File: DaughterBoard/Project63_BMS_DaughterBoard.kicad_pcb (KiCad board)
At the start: 4 copper layers, 166 parts, among them J1 430450200, J4 1-794106-0, J5 430450200, Q1 ZXTN4004KTC, U1 BQ79614PAPRQ1

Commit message: Initial Routing
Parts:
- D1, D2: footprint PESD1CAN,215:SOT23_PESD1_NEX -> PESD1CAN_215:SOT23_PESD1_NEX
- moved TP5 5.40 mm to (157.5, 76.2)
- turned R28 to 0 degrees
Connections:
- C3 pad 2: REFHF -> REFHP
- F30 pad 1: Cell 14S -> BAT
- J4 pad 18: Cell 14S -> BAT
- R1 pad 2: Cell 14S -> BAT
- R33 pad 2: Cell 14S -> BAT
- U1 pad 36: REFHP -> AVSS
- U1 pad 37: REFHF -> REFHP
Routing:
- net BAT: track 0.00 -> 133.5 mm, vias 0 -> 2
- net Cell 0: track 0.00 -> 102.9 mm
- net VC0: track 0.00 -> 67.3 mm
- net Cell 14: track 0.00 -> 55.0 mm, vias 0 -> 1
- net VC1: track 0.00 -> 52.3 mm
- net VC2: track 0.00 -> 45.2 mm
- net Cell 6: track 0.00 -> 43.1 mm, vias 0 -> 2
- net Net-(F2-Pad2): track 0.00 -> 42.1 mm
- net Net-(F1-Pad2): track 0.00 -> 42.1 mm
- net Net-(F15-Pad2): track 0.00 -> 40.3 mm
- net Net-(F3-Pad2): track 0.00 -> 39.7 mm
- net VC3: track 0.00 -> 39.2 mm
- net Net-(F14-Pad2): track 0.00 -> 39.1 mm
- net Net-(F4-Pad2): track 0.00 -> 35.7 mm
- net Net-(F13-Pad2): track 0.00 -> 34.8 mm
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
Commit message: Routing update 2
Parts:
- moved TP6 50.1 mm to (160.0, 68.6)
- moved J4 35.6 mm to (55.0, 116.3)
- moved TP1 31.0 mm to (146.0, 73.3)
- moved R33 30.9 mm to (124.5, 55.9), turned to 180 degrees
- moved TP11 29.9 mm to (151.1, 73.3)
- moved R32 29.0 mm to (132.1, 55.9)
- moved R10 28.4 mm to (110.7, 123.2), turned to -90 degrees
- moved R2 28.4 mm to (110.6, 82.6), turned to -90 degrees
- moved R3 28.4 mm to (110.6, 87.7), turned to -90 degrees
- moved R4 28.4 mm to (110.6, 92.7), turned to -90 degrees
- moved R5 28.4 mm to (110.6, 97.8), turned to -90 degrees
- moved R6 28.4 mm to (110.6, 102.9), turned to -90 degrees
- moved R8 28.4 mm to (110.6, 113.1), turned to -90 degrees
- moved R9 28.4 mm to (110.6, 118.1), turned to -90 degrees
- moved R11 28.4 mm to (110.6, 128.3), turned to -90 degrees
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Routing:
- net CB0: track 0.00 -> 92.6 mm, vias 0 -> 2
- net CB1: track 0.00 -> 81.1 mm, vias 0 -> 2
- net CB2: track 0.00 -> 71.6 mm, vias 0 -> 2
- net CB3: track 0.00 -> 63.6 mm, vias 0 -> 2
- net CB4: track 0.00 -> 57.4 mm, vias 0 -> 2
- net CB5: track 0.00 -> 50.5 mm, vias 0 -> 2
- net CB6: track 0.00 -> 49.2 mm, vias 0 -> 2
- net CB7: track 0.00 -> 43.3 mm, vias 0 -> 2
- net CB14: track 0.00 -> 40.4 mm
- net CB13: track 0.00 -> 38.9 mm
- net CB9: track 0.00 -> 38.7 mm, vias 0 -> 2
- net CB8: track 0.00 -> 38.2 mm, vias 0 -> 2
- net Cell 0: track 102.9 -> 65.2 mm
- net CB12: track 0.00 -> 37.4 mm, vias 0 -> 2
- net CB11: track 0.00 -> 36.6 mm, vias 0 -> 2
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
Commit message: Routing Update 3
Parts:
- C10, C11, C12, C13, C14, C15, C16, C17, C18, C19, C2, C3, C31, C32, C33, C34, C4, C5, C6, C7, C9: moved to B.Cu
- R1: value 30 -> 30
- R10, R11, R12, R2, R24, R25, R26, R27, R3, R4, R5, R6, R7, R8, R9: value 7.5 -> 7.5
- R13, R14, R15, R16, R17, R18, R19, R20, R21, R22, R23, R28, R29, R30, R31, R32: value 100 -> 100
- R33: value 200 -> 200
- R34, R35, R41, R42: value 51 -> 51
- R37, R38, R39, R40, R43, R44, R45, R46, R47, R48, R50, R51, R52, R53, R54, R55: value 0 -> 0
- moved J1 52.1 mm to (210.8, 117.3)
- moved R44 49.2 mm to (213.4, 109.2)
- moved LDOIN 48.3 mm to (186.2, 35.3)
- moved R43 47.3 mm to (208.3, 109.2)
- moved R47 45.9 mm to (205.8, 103.5)
- moved FL1 45.4 mm to (210.7, 103.3)
- moved TSREF 45.1 mm to (190.5, 66.0)
- moved R42 44.8 mm to (213.2, 68.0)
- moved R48 44.8 mm to (215.8, 103.6)
- moved C43 44.6 mm to (213.3, 95.9)
- moved C44 44.5 mm to (208.1, 95.9)
- moved R39 43.3 mm to (213.2, 62.9)
- moved R45 43.0 mm to (208.2, 91.1)
- moved R46 43.0 mm to (213.3, 91.1)
- moved R38 42.3 mm to (208.2, 88.2)
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- renumbered TP7 to AVDD, TP5 to BAT, TP32 to CELL0, TP27 to CELL1, TP18 to CELL10, TP28 to CELL11, TP29 to CELL12, TP30 to CELL13, TP31 to CELL14, TP26 to CELL2, TP25 to CELL3, TP24 to CELL4, TP23 to CELL5, TP22 to CELL6, TP21 to CELL7, TP20 to CELL8, TP19 to CELL9, TP9 to CVDD, TP11 to DVDD, TP2 to LDOIN, TP3 to NEG5V, TP14 to NFAULT, TP4 to NPNB, TP6 to REFHP, TP1 to TSREF
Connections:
- net COMML_N_OPT renamed COMML_N_OPT-
- net COMML_P_OPT renamed COMML_P_OPT+
- C2 pad 1: AVSS -> CVSS
- C3 pad 1: AVSS -> REFHM
- C40 pad 1: AVSS -> CVSS
- C41 pad 1: AVSS -> CVSS
- C42 pad 1: AVSS -> CVSS
- C42 pad 2: COMHN -> COMHP
- C45 pad 1: AVSS -> CVSS
- C45 pad 2: COMHP -> COMHN
- C5 pad 1: AVSS -> CVSS
- C6 pad 1: AVSS -> CVSS
- C7 pad 1: AVSS -> DVSS
- C8 pad 1: AVSS -> CVSS
- D1 pad 3: AVSS -> CVSS
- D2 pad 3: AVSS -> CVSS
- R34 pad 2: Net-(D2-Pad1) -> Net-(D2-Pad2)
- R35 pad 2: Net-(D2-Pad2) -> Net-(D2-Pad1)
- R37 pad 2: Net-(D2-Pad2) -> Net-(D2-Pad1)
- R38 pad 2: Net-(D2-Pad1) -> Net-(D2-Pad2)
- R39 pad 1: COMMH_N_OPT -> COMMH_N_OPT-
- R40 pad 1: COMMH_P_OPT -> COMMH_P_OPT+
- R50 pad 2: ISO_COMMH_P -> ISO_COMMH_N
- R51 pad 2: ISO_COMMH_N -> ISO_COMMH_P
- R54 pad 1: COMMH_P_OPT -> COMMH_N_OPT-
- R55 pad 1: COMMH_N_OPT -> COMMH_P_OPT+
- U1 pad 36: AVSS -> REFHM
- U1 pad 46: AVSS -> CVSS
- U1 pad 50: AVSS -> DVSS
- U1 pad 62: unconnected-(U1-Pad62) -> NFAULT
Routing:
- net LDOIN: track 0.00 -> 43.0 mm, vias 0 -> 2
- net COMLN: track 0.00 -> 35.1 mm
- net COMHN: track 0.00 -> 34.9 mm
- net COMHP: track 0.00 -> 34.9 mm
- net COMLP: track 0.00 -> 34.9 mm
- net NPNB: track 7.31 -> 40.7 mm, vias 0 -> 2
- net AVSS: track 0.00 -> 28.2 mm, vias 0 -> 1
- net NEG5V: track 0.00 -> 23.2 mm, vias 0 -> 1
- net CVDD: track 0.00 -> 21.4 mm, vias 0 -> 1
- net REFHP: track 0.00 -> 18.7 mm, vias 0 -> 1
- net TSREF: track 0.00 -> 14.6 mm, vias 0 -> 1
- net VC10: track 43.7 -> 29.6 mm, vias 2 -> 0
- net REFHM: track 0.00 -> 13.2 mm, vias 0 -> 1
- net CB0: track 92.6 -> 79.7 mm
- net Cell 7: track 42.1 -> 30.0 mm
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
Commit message: Silkscreen edits
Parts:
- moved AVDD 20.3 mm to (190.4, 101.6)
- moved C1 20.3 mm to (168.2, 89.8)
- moved C10 20.3 mm to (170.6, 104.8)
- moved C11 20.3 mm to (172.2, 106.2)
- moved C13 20.3 mm to (175.3, 106.2)
- moved C15 20.3 mm to (178.7, 106.3)
- moved C16 20.3 mm to (179.2, 104.8)
- moved C17 20.3 mm to (183.9, 103.4)
- moved C18 20.3 mm to (185.5, 101.1)
- moved C19 20.3 mm to (185.5, 98.6)
- moved C2 20.3 mm to (186.6, 94.2)
- moved C20 20.3 mm to (166.4, 102.4)
- moved C21 20.3 mm to (170.5, 104.8)
- moved C22 20.3 mm to (172.0, 106.2)
- moved C24 20.3 mm to (175.0, 106.2)
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- renumbered LDOIN to TP2, NPNB to TP4
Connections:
- C40 pad 1: CVSS -> AVSS
- C41 pad 1: CVSS -> AVSS
- C42 pad 1: CVSS -> AVSS
- C45 pad 1: CVSS -> AVSS
- U1 pad 2: unconnected-(U1-Pad2) -> /BQ79614_Bootstrapping/Cell 14S PIN
- U1 pad 3: unconnected-(U1-Pad3) -> /BQ79614_Bootstrapping/Cell 14S PIN
- U1 pad 4: unconnected-(U1-Pad4) -> /BQ79614_Bootstrapping/Cell 14S PIN
- U1 pad 5: unconnected-(U1-Pad5) -> /BQ79614_Bootstrapping/Cell 14S PIN
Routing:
- net CVSS: track 0.00 -> 19.1 mm, vias 0 -> 1
- net /BQ79614_Bootstrapping/Cell 14S PIN: track 13.6 -> 15.6 mm
- net REFHM: track 13.2 -> 14.5 mm, vias 1 -> 2
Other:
- board outline added: 162.6 x 114.3 mm

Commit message: Updates
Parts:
- C39: value 0.22µF -> 0.22uF
- C7: moved to F.Cu
- moved TP5 54.1 mm to (111.1, 79.0)
- moved TP9 26.6 mm to (177.8, 67.3)
- moved TP2 17.9 mm to (171.4, 66.0), turned to 90 degrees
- moved TP3 16.9 mm to (181.6, 77.5)
- moved Q1 14.4 mm to (168.9, 72.3), turned to 90 degrees
- moved TP4 7.99 mm to (175.3, 63.5), turned to 90 degrees
- moved C5 6.87 mm to (190.5, 94.0), turned to 90 degrees
- moved TP7 5.13 mm to (190.5, 106.7)
- moved C6 2.58 mm to (187.9, 94.0)
- moved C18 2.45 mm to (185.5, 103.5)
- moved C28 2.32 mm to (185.5, 103.3)
- moved C29 2.23 mm to (185.5, 100.8)
- moved C30 2.18 mm to (187.2, 100.8)
- moved C4 2.18 mm to (187.2, 100.5), turned to 90 degrees
- moved C19 1.89 mm to (185.5, 100.5)
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- renumbered TSREF to TP1, DVDD to TP11, NFAULT to TP14, CELL10 to TP18, CELL9 to TP19, CELL8 to TP20, CELL7 to TP21, CELL6 to TP22, CELL5 to TP23, CELL4 to TP24, CELL3 to TP25, CELL2 to TP26, CELL1 to TP27, CELL11 to TP28, CELL12 to TP29, NEG5V to TP3, CELL13 to TP30, CELL14 to TP31, CELL0 to TP32, BAT to TP5, REFHP to TP6, AVDD to TP7, CVDD to TP9
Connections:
- C2 pad 1: CVSS -> AVSS
- C3 pad 1: REFHM -> AVSS
- C5 pad 1: CVSS -> AVSS
- C6 pad 1: CVSS -> AVSS
- C7 pad 1: DVSS -> AVSS
- C8 pad 1: CVSS -> AVSS
- D1 pad 3: CVSS -> AVSS
- D2 pad 3: CVSS -> AVSS
- U1 pad 36: REFHM -> AVSS
- U1 pad 46: CVSS -> AVSS
- U1 pad 50: DVSS -> AVSS
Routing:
- net BAT: track 114.6 -> 36.1 mm, vias 2 -> 1
- net CVSS: track 19.1 -> 0.00 mm, vias 1 -> 0
- net CVDD: track 21.4 -> 37.4 mm, vias 1 -> 2
- net REFHM: track 14.5 -> 0.00 mm, vias 2 -> 0
- net AVSS: track 28.2 -> 42.3 mm, vias 1 -> 3
- net Net-(Q1-C): track 26.6 -> 13.2 mm, vias 2 -> 0
- net TSREF: track 14.6 -> 22.8 mm
- net LDOIN: track 43.0 -> 35.2 mm
- net DVSS: track 5.30 -> 0.00 mm, vias 1 -> 0
- net DVDD: track 10.0 -> 5.36 mm, vias 1 -> 0
- net AVDD: track 11.4 -> 15.7 mm
- net VC2: track 61.3 -> 57.2 mm
- net NPNB: track 40.7 -> 37.1 mm, vias 2 -> 3
- net VC0: track 77.3 -> 75.1 mm
- net CB0: track 79.7 -> 77.7 mm
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- added copper zone on F.Cu, net AVSS
- added copper zone on In1.Cu, net AVSS
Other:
- board size 162.6 x 114.3 mm -> 175.3 x 114.3 mm

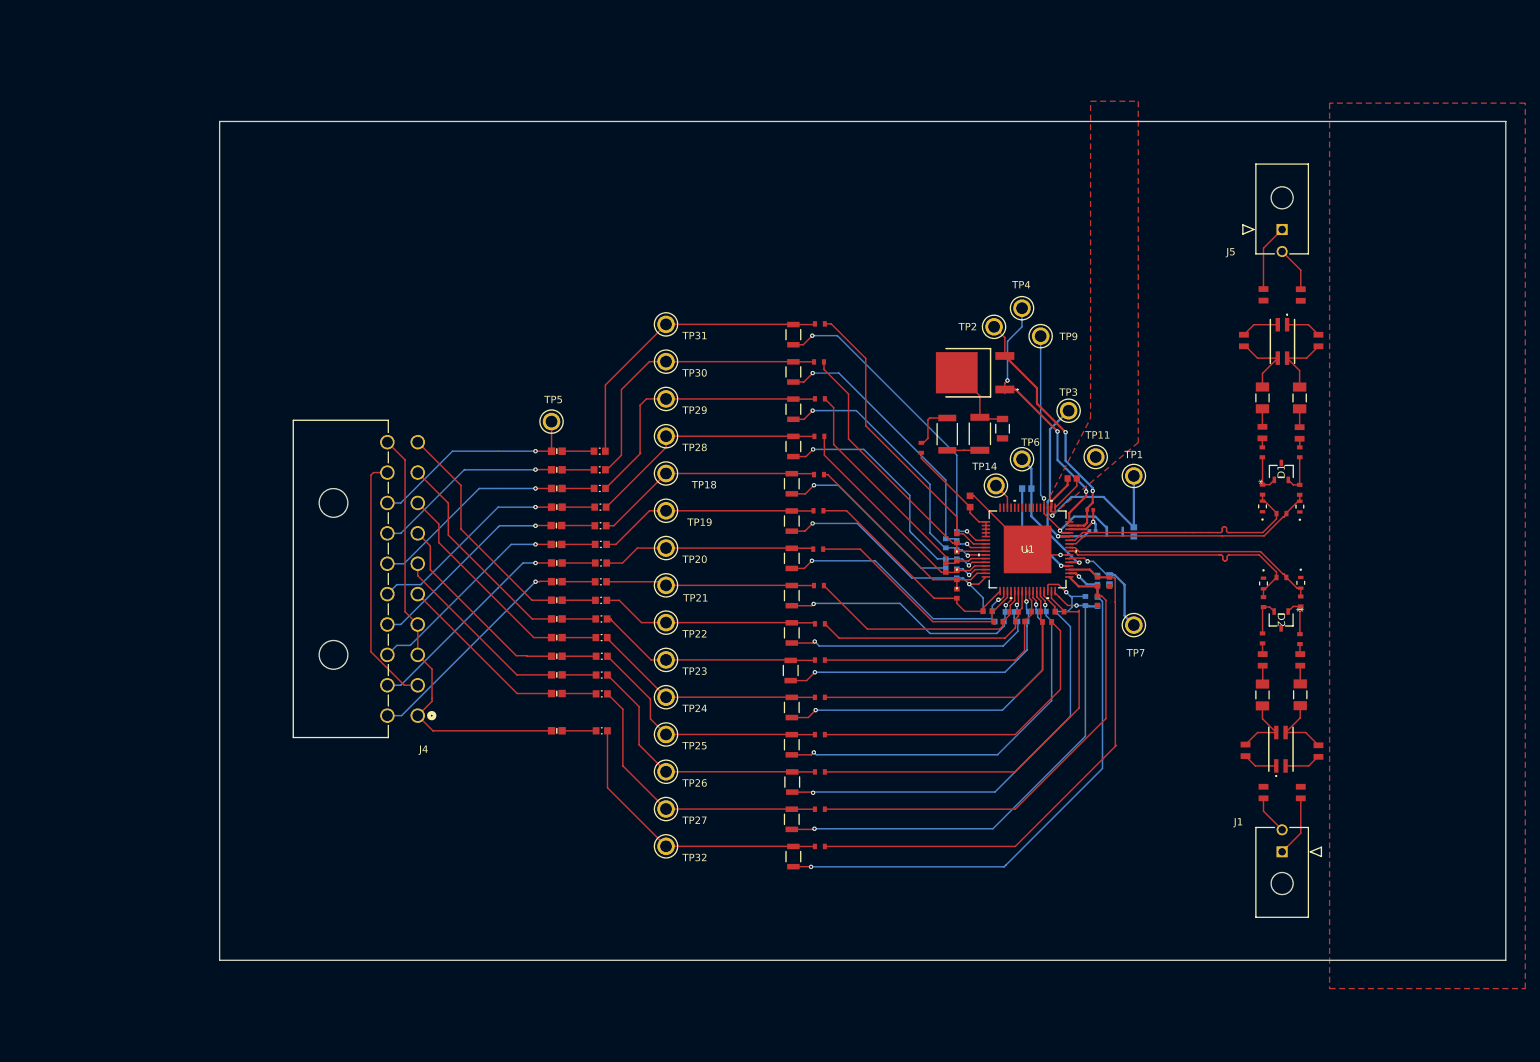
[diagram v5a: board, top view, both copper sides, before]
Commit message: Reworked ground planes
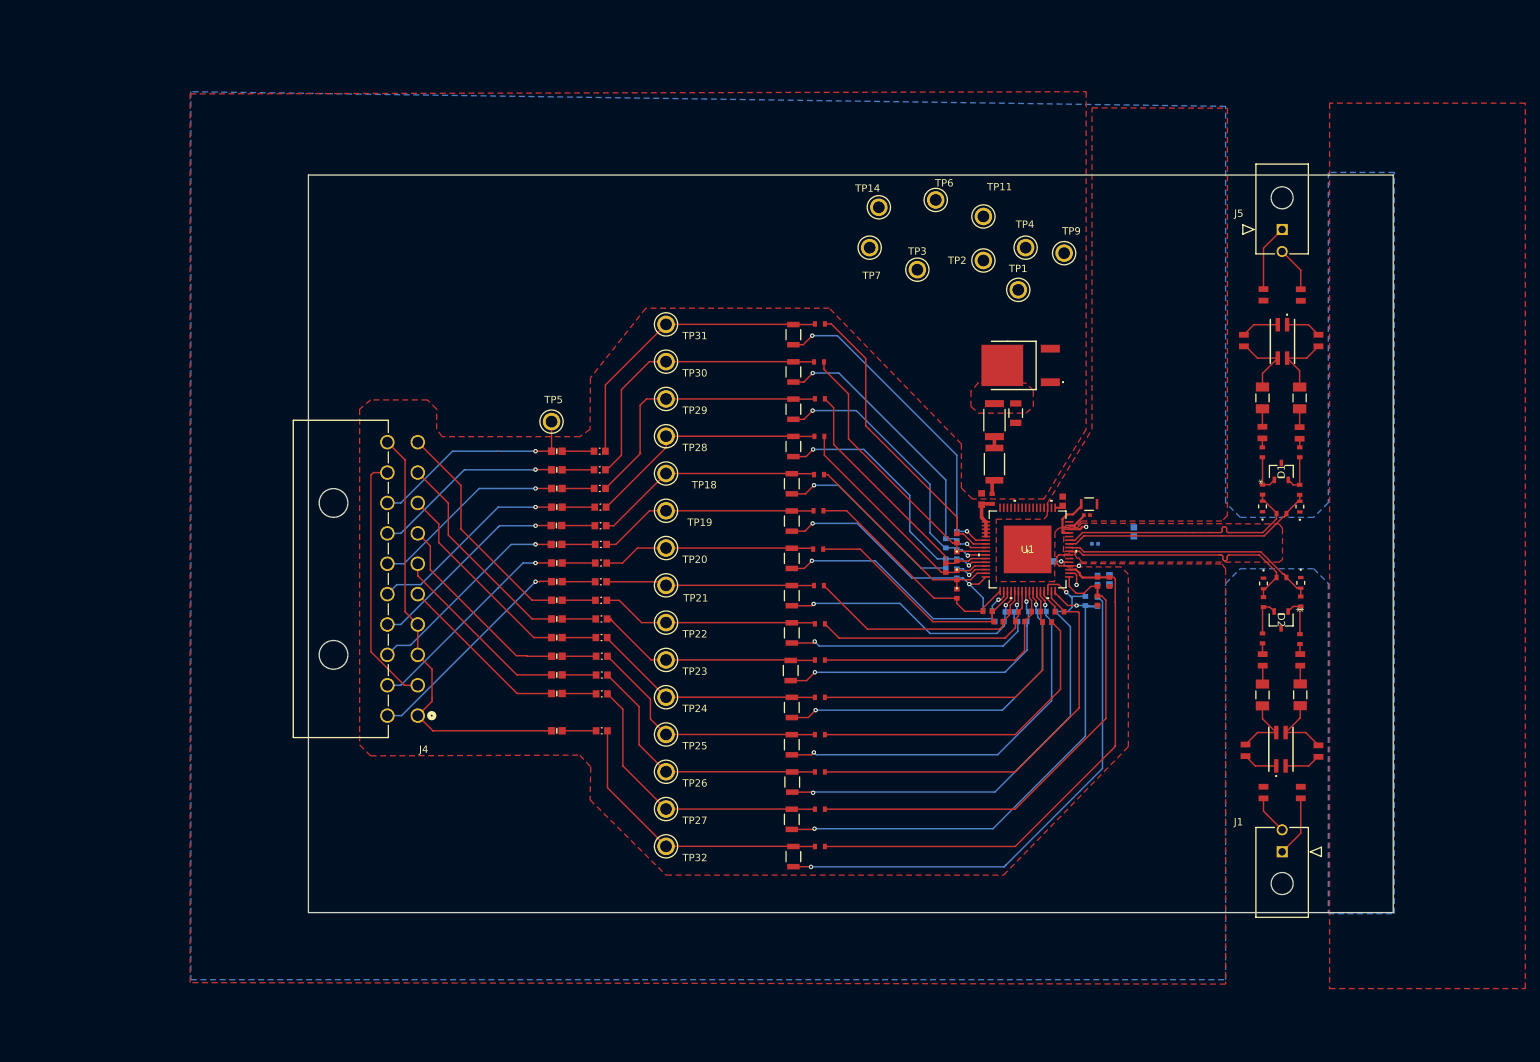
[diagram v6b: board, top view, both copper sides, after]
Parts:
- C6: moved to F.Cu
- moved TP7 62.8 mm to (154.5, 55.2)
- moved TP14 41.1 mm to (155.8, 49.8)
- moved TP6 37.2 mm to (163.5, 48.8)
- moved TP11 36.2 mm to (170.0, 51.0)
- moved TP1 29.9 mm to (174.8, 61.0)
- moved TP3 28.2 mm to (161.0, 58.2)
- moved R1 11.9 mm to (171.2, 89.5)
- moved TP9 11.8 mm to (181.0, 56.0)
- moved C3 10.4 mm to (178.9, 98.0)
- moved TP2 9.16 mm to (170.0, 57.0)
- moved TP4 8.26 mm to (175.8, 55.2)
- moved R33 7.61 mm to (171.5, 84.8), turned to -90 degrees
- moved Q1 6.28 mm to (175.1, 71.3)
- moved C6 5.15 mm to (184.4, 90.2)
- moved C7 3.36 mm to (180.8, 89.8), turned to -90 degrees
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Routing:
- net NPNB: track 37.1 -> 0.00 mm, vias 3 -> 0
- net AVSS: track 42.3 -> 9.41 mm, vias 3 -> 2
- net LDOIN: track 35.2 -> 2.64 mm, vias 2 -> 0
- net CVDD: track 37.4 -> 6.38 mm, vias 2 -> 0
- net NEG5V: track 25.0 -> 0.00 mm, vias 1 -> 0
- net TSREF: track 22.8 -> 0.00 mm, vias 1 -> 0
- net REFHP: track 18.9 -> 2.22 mm
- net AVDD: track 15.7 -> 0.31 mm, vias 1 -> 0
- net Net-(Q1-C): track 13.2 -> 0.00 mm
- net /BQ79614_Bootstrapping/Cell 14S PIN: track 15.6 -> 6.02 mm
- net BAT: track 36.1 -> 31.7 mm
- net DVDD: track 5.36 -> 1.14 mm
- net NFAULT: track 3.67 -> 0.00 mm
- net CB0: track 77.7 -> 74.2 mm
- net Net-(R32-Pad1): track 4.45 -> 1.55 mm
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- added copper zone on B.Cu, net AVSS
- added copper zone on F.Cu, net Net-(Q1-C)
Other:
- board size 175.3 x 114.3 mm -> 147.8 x 100.5 mm

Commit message: Finished board
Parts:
- removed D1, D2: 24V, PESD1CAN_215:SOT23_PESD1_NEX
- added D701: 24V, Package_TO_SOT_SMD:SOT-23, F.Cu at (197.4, 94.9)
- added D702: 24V, Package_TO_SOT_SMD:SOT-23, F.Cu at (197.5, 76.2)
- added G***: LOGO, LOGO, F.Cu at (84.9, 51.9)
- added H101: MountingHole, MountingHole:MountingHole_3.2mm_M3, F.Cu at (70.0, 40.0)
- added H102: MountingHole, MountingHole:MountingHole_3.2mm_M3, F.Cu at (210.0, 40.0)
- added H103: MountingHole, MountingHole:MountingHole_3.2mm_M3, F.Cu at (70.0, 130.0)
- added H104: MountingHole, MountingHole:MountingHole_3.2mm_M3, F.Cu at (210.0, 130.0)
- moved TP505 48.2 mm to (179.7, 96.3)
- moved TP507 46.1 mm to (179.8, 91.9)
- moved TP506 31.2 mm to (184.4, 78.9)
- moved C205 30.0 mm to (165.1, 78.0), turned to 0 degrees
- moved TP508 25.2 mm to (166.4, 72.6)
- moved TP504 23.6 mm to (179.0, 78.8)
- moved C202 19.9 mm to (167.8, 85.9)
- moved TP503 19.3 mm to (174.4, 74.1)
- moved TP510 17.6 mm to (98.1, 67.2)
- moved C322 17.3 mm to (174.0, 89.5), turned to -90 degrees
- moved C206 17.2 mm to (172.0, 78.3)
- moved TP502 17.0 mm to (162.4, 72.6)
- moved C303 16.7 mm to (159.1, 95.8)
- moved C308 16.7 mm to (166.1, 94.5)
- moved C313 16.7 mm to (157.4, 94.4)
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- renumbered C1 to C201, C2 to C202, C3 to C203, C4 to C204, C5 to C205, C6 to C206, C7 to C207, C8 to C208, C9 to C301, C10 to C302, C11 to C303, C12 to C304, C13 to C305, C14 to C306, C15 to C307, C16 to C308, C17 to C309, C18 to C310, C19 to C311, C20 to C312, C21 to C313, C22 to C314, C23 to C315, C24 to C316, C25 to C317, C26 to C318, C27 to C319, C28 to C320, C29 to C321, C30 to C322, C31 to C323, C32 to C324, C33 to C325, C34 to C326, C35 to C327, C36 to C328, C37 to C329, C38 to C330, C39 to C601, C44 to C701, C43 to C702, C41 to C703, C40 to C704, C45 to C705, C42 to C706, C46 to C707, C47 to C708, F26 to F301, F25 to F302, F24 to F303, F23 to F304, F22 to F305, F21 to F306, F20 to F307, F19 to F308, F18 to F309, F17 to F310, F16 to F311, F11 to F312, F10 to F313, F9 to F314, F8 to F315, F7 to F316, F2 to F317, F6 to F318, F5 to F319, F4 to F320, F3 to F321, F1 to F322, F30 to F323, F29 to F324, F28 to F325, F27 to F326, F15 to F327, F14 to F328, F13 to F329, F12 to F330, FL1 to FL701, FL2 to FL702, J4 to J401, J1 to J701, J5 to J702, Q1 to Q601, R1 to R201, R2 to R301, R3 to R302, R4 to R303, R5 to R304, R6 to R305, R7 to R306, R8 to R307, R9 to R308, R10 to R309, R11 to R310, R12 to R311, R13 to R312, R14 to R313, R15 to R314, R16 to R315, R17 to R316, R18 to R317, R19 to R318, R20 to R319, R21 to R320, R22 to R321, R23 to R322, R27 to R323, R26 to R324, R25 to R325, R24 to R326, R29 to R327, R30 to R328, R31 to R329, R28 to R330, R32 to R601, R33 to R602, R43 to R701, R44 to R702, R37 to R703, R38 to R704, R47 to R705, R48 to R706, R34 to R707, R35 to R708, R45 to R709, R46 to R710, R36 to R711, R49 to R712, R54 to R713, R55 to R714, R52 to R715, R53 to R716, R41 to R717, R42 to R718, R40 to R719, R39 to R720, R50 to R721, R51 to R722, TP32 to TP301, TP18 to TP302, TP19 to TP303, TP20 to TP304, TP21 to TP305, TP22 to TP306, TP23 to TP307, TP24 to TP308, TP25 to TP309, TP26 to TP310, TP27 to TP311, TP31 to TP312, TP30 to TP313, TP29 to TP314, TP28 to TP315, TP11 to TP501, TP1 to TP502, TP9 to TP503, TP2 to TP504, TP7 to TP505, TP3 to TP506, TP6 to TP507, TP14 to TP508, TP4 to TP509, TP5 to TP510, U1 to U201
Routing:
- net BAT: track 31.7 -> 116.5 mm
- net LDOIN: track 2.64 -> 35.2 mm, vias 0 -> 7
- net NEG5V: track 0.00 -> 23.3 mm, vias 0 -> 1
- net NPNB: track 0.00 -> 23.0 mm, vias 0 -> 2
- net AVSS: track 9.41 -> 29.8 mm, vias 2 -> 132
- net DVDD: track 1.14 -> 18.9 mm
- net AVDD: track 0.31 -> 15.9 mm, vias 0 -> 1
- net REFHP: track 2.22 -> 17.1 mm
- net CVDD: track 6.38 -> 20.6 mm, vias 0 -> 3
- net NFAULT: track 0.00 -> 10.3 mm
- net TSREF: track 0.00 -> 8.97 mm, vias 0 -> 1
- net CB0: track 74.2 -> 79.9 mm
- net Net-(FL702-N2+): track 5.22 -> 9.27 mm
- net Net-(FL702-N1+): track 4.84 -> 8.87 mm
- net Net-(FL701-N2+): track 4.99 -> 8.55 mm
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- added copper zone on F.Cu, net /BQ79614_Bootstrapping/Cell 14S PIN
- added copper zone on In2.Cu, net AVSS
- added copper zone on B.Cu, net LDOIN
- added copper zone on F.Cu, net LDOIN
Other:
- board size 147.8 x 100.5 mm -> 150 x 100 mm
- board text added: "COMMH+"
- board text added: "COMMH-"
- board text added: "COMML+"
- board text added: "COMML-"

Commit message: Daughterboard 100% Complete + Edited Motherboard BOM
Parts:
- removed TP510: 5012, 5012:TP_5012
- F301, F302, F303, F304, F305, F306, F307, F308, F309, F310, F311, F323, F324, F325, F326: footprint 0438.250WRA:FUSC1608X61N -> Fuse:Fuse_0603_1608Metric
- moved F311 0.06 mm to (98.7, 110.8)
- renumbered TP312 to BAT_POSITIVE301, TP313 to TP312, TP314 to TP313, TP315 to TP314
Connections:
- net /BQ79614_Bootstrapping/Cell 14S PIN renamed Net-(C201-Pad2)
- F311 pad 1: Cell 0 -> Cell 0S
- F323 pad 1: BAT -> Cell 14S
- J401 pad 1: Cell 0 -> AVSS
- J401 pad 18: BAT -> Cell 14S
- J401 pad 19: Cell 14 -> BAT
- J401 pad 2: Cell 14 -> BAT
- J401 pad 20: Cell 0 -> AVSS
- J401 pad 3: Cell 0 -> AVSS
- J401 pad 4: Cell 0 -> Cell 0S
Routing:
- net Cell 0: track 59.8 -> 0.00 mm
- net Cell 14: track 34.8 -> 0.00 mm
- net BAT: track 116.5 -> 150.3 mm, vias 1 -> 0
- net Cell 14S: track 0.00 -> 25.2 mm, vias 0 -> 1
- net Cell 0S: track 0.00 -> 24.1 mm
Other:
- board text added: "BAT NEGATIVE (Cell 1-)"
- board text added: "BAT POSITIVE (Cell 14+)"
- board text added: "Cell 1+"
- board text added: "Cell 10+"
- board text added: "Cell 11+"
- board text added: "Cell 12+"
- board text added: "Cell 13+"
- board text added: "Cell 2+"
- board text added: "Cell 3+"
- board text added: "Cell 4+"
- board text added: "Cell 5+"
- board text added: "Cell 6+"
- board text added: "Cell 7+"
- board text added: "Cell 8+"
- board text added: "Cell 9+"
